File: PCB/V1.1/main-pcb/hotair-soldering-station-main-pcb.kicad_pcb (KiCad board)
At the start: 2 copper layers, 89.4 x 90.9 mm, 84 parts, among them J1 230VAC_IN, J10 SOLD_IRON (r.2,54), J13 ICP (goldpin r2,54), J2 main-board-conn, J3 EARTH_GND, J4 24V_IN (NS-25 r2,54), J5 PSUPPLY (PWZ-02S r.3,96), J6 HOTAIR_FAN (JST r,2,54), J7 HOTAIR_MEAS (JST r.2,5), J8 HOTAIR_HEATER (PWZ-02S r.3,96), J9 SOLD_IRON (r.2,54), Q1 BC817, Q10 FP3055LP, Q2 BC807, Q3 BC817, Q4 Q_PMOS_GDS, Q5 BC817, Q6 BT139-600, Q7 BC817, Q8 FP3055LP, Q9 BC817, U1 MOC3041M, U2 MAX31855KASA, U3 MP1584-Step-Down, U4 AP1117-ADJ, U5 STM32F030K6Tx, U6 LM358, U7 MAX31855KASA, U8 STM32F103C6Tx

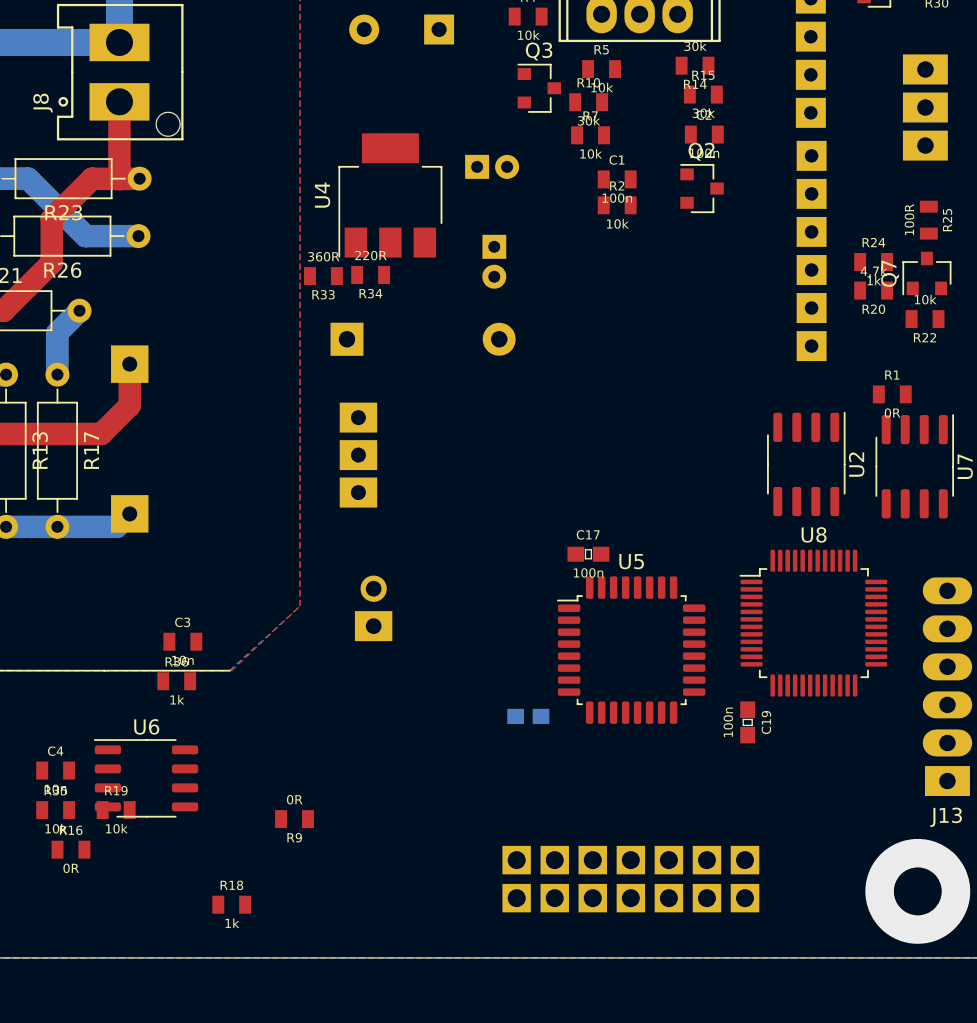
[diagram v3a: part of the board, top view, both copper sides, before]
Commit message: Pin assign to new STM32F103, front panel design to new case
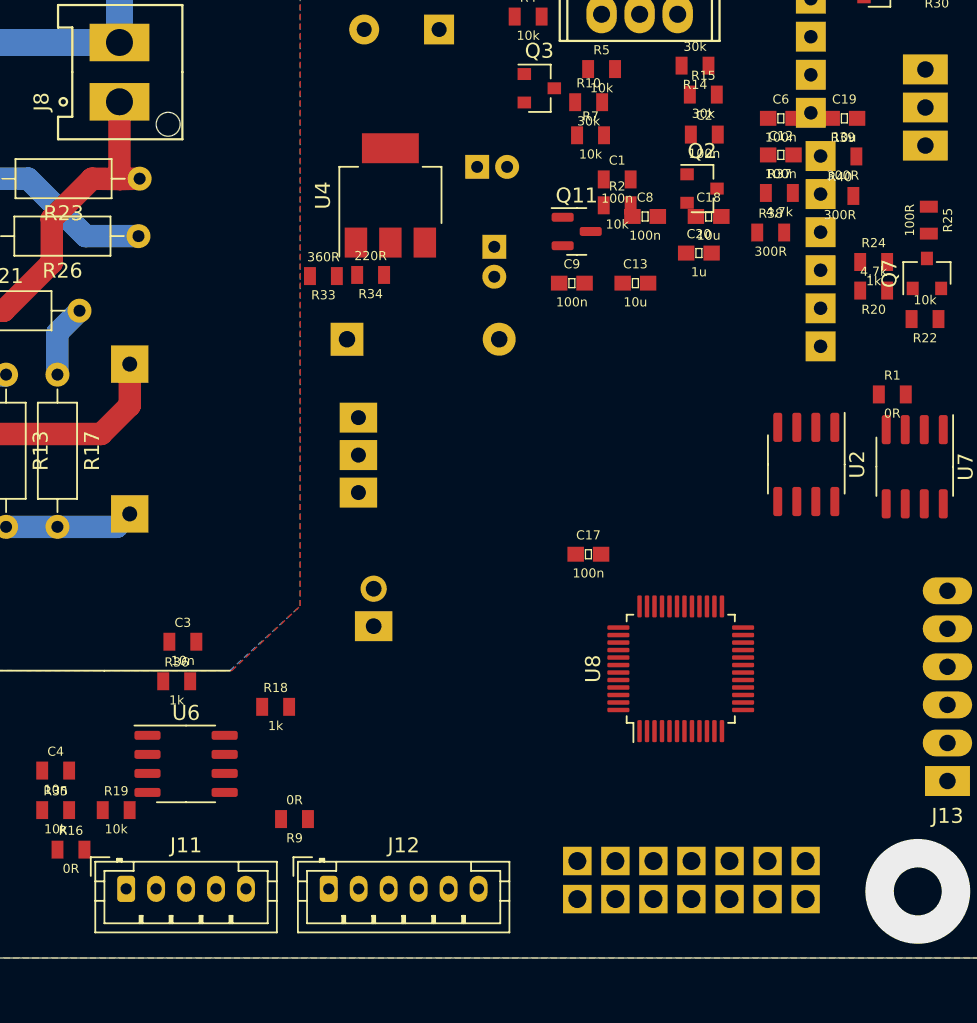
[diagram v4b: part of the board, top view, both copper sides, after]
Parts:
- removed U5: STM32F030K6Tx, Package_QFP:LQFP-32_7x7mm_P0.8mm
- added C12: 100n, Capacitors:0603, F.Cu at (92.4, 55.2)
- added C13: 10u, Capacitors:0603, F.Cu at (82.7, 63.8)
- added C20: 1u, Capacitors:0603, F.Cu at (86.9, 61.8)
- added C6: 100n, Capacitors:0603, F.Cu at (92.4, 52.8)
- added C8: 100n, Capacitors:0603, F.Cu at (83.3, 59.3)
- added C9: 100n, Capacitors:0603, F.Cu at (78.5, 63.8)
- added J11: LCD_CON2 (JST r.2.0), Connector_JST:JST_PH_B5B-PH-K_1x05_P2.00mm_Vertical, F.Cu at (48.7, 104.2)
- added J12: LCD_CON1 (JST r.2.0), Connector_JST:JST_PH_B6B-PH-K_1x06_P2.00mm_Vertical, F.Cu at (62.2, 104.2)
- added Q11: BC817, Package_TO_SOT_SMD:SOT-23, F.Cu at (78.8, 60.3)
- added R37: 4,7k, Capacitors:0805, F.Cu at (92.3, 57.8)
- added R38: 300R, Capacitors:0805, F.Cu at (91.7, 60.4)
- added R39: 300R, Capacitors:0805, F.Cu at (96.5, 55.3)
- added R40: 300R, Capacitors:0805, F.Cu at (96.3, 58.0)
- C18: value 100n -> 10u; moved to F.Cu
- C19: value 100n -> 10u
- J2: value main-board-conn -> FRONT_PANEL (IDC r. 2,54)
- moved C19 40.8 mm to (96.6, 52.8), turned to 0 degrees
- moved C18 35.5 mm to (87.6, 59.3)
- moved R18 13.5 mm to (58.7, 92.1)
- moved U8 9.40 mm to (85.7, 89.5), turned to 90 degrees
- moved J2 4.05 mm to (77.1, 100.5)
- moved U6 2.81 mm to (52.7, 95.9)
- moved J9 0.60 mm to (91.8, 54.0)
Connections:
- net HOTAIR_ADC renamed HOTAIR_TEMP_ADC
- C2 pad 1: FAN_ADC -> HOTAIR_FAN_ADC
- J10 pad 4: IRON_T12_HEATER -> IRON_T12_MOTION_SW
- J2 pad 10: HOTAIR_ON_SW -> HOTAIR_UP_SW
- J2 pad 11: SOLDER_ON_SW -> HOTAIR_DOWN_SW
- J2 pad 12: SPI1_SCK -> SOLDER_SELECT_SW
- J2 pad 13: (no net) -> HOTAIR_ON_SW
- J2 pad 14: SPI1_MOSI -> SOLDER_ON_SW
- J2 pad 3: GND -> MENU_UP_SW
- J2 pad 4: SOLDER_DOWN_SW -> MENU_OK_SW
- J2 pad 5: SOLDER_UP_SW -> MENU_DOWN_SW
- J2 pad 6: HOTAIR_DOWN_SW -> SOLDER_DOWN_SW
- J2 pad 7: HOTAIR_UP_SW -> SOLDER_UP_SW
- R14 pad 1: FAN_ADC -> HOTAIR_FAN_ADC
- R15 pad 2: FAN_ADC -> HOTAIR_FAN_ADC
- R2 pad 1: FAN_PWM -> HOTAIR_FAN_PWM
- R36 pad 2: IRON_T12_ADC -> IRON_T12_TEMP_ADC
- U1 pad 3: (no net) -> unconnected-(U1-Pad3)
- U1 pad 5: (no net) -> unconnected-(U1-Pad5)
- U7 pad 6: (no net) -> MAX31855_IRON_WEP_CS
- U8 pad 1: (no net) -> +3V3
- U8 pad 10: IRON_T12_ADC -> HOTAIR_FAN_ADC
- U8 pad 12: SOLDER_DOWN_SW -> UART_DBG_TX
- U8 pad 13: FAN_ADC -> MAX31855_HOTAIR_CS
- U8 pad 14: BUZZER -> MAX31855_IRON_CS
- U8 pad 17: SPI1_MOSI -> IRON_WEP_HEATER_CTRL
- U8 pad 18: SOLDER_ON_SW -> IRON_T12_TEMP_ADC
- U8 pad 19: HOTAIR_REED_SW -> IRON_T12_MOTION_SW
- U8 pad 2: (no net) -> LCD_RW
- U8 pad 20: (no net) -> HOTAIR_REED_SW
- U8 pad 21: (no net) -> SOLDER_ON_SW
- U8 pad 22: (no net) -> SOLDER_UP_SW
- U8 pad 25: (no net) -> SOLDER_DOWN_SW
- U8 pad 26: (no net) -> SOLDER_SELECT_SW
- U8 pad 27: (no net) -> HOTAIR_DOWN_SW
- U8 pad 28: (no net) -> HOTAIR_UP_SW
- U8 pad 29: HOTAIR_UP_SW -> HOTAIR_FAN_PWM
- U8 pad 3: (no net) -> LCD_RS
- U8 pad 30: UART_DBG_TX -> HOTAIR_HEATER_CTRL
- U8 pad 31: HOTAIR_FAN_UP_SW -> MENU_UP_SW
- U8 pad 32: HOTAIR_FAN_DOWN_SW -> MENU_OK_SW
- U8 pad 33: HOTAIR_ON_SW -> MENU_DOWN_SW
- U8 pad 38: MAX31855_HOTAIR_CS -> BUZZER
- U8 pad 39: SOLDER_UP_SW -> LCD_BACKLIGHT_PWM
- U8 pad 4: (no net) -> HOTAIR_FAN_DOWN_SW
- U8 pad 40: HOTAIR_DOWN_SW -> LCD_D7
- U8 pad 41: (no net) -> LCD_D6
- U8 pad 42: IRON_WEP_HEATER_CTRL -> IRON_T12_HEATER_CTRL
- U8 pad 43: FAN_PWM -> LCD_D5
- U8 pad 44: GND -> unconnected-(U8-Pad44)
- U8 pad 45: IRON_T12_HEATER_CTRL -> LCD_D4
- U8 pad 46: HOTAIR_HEATER_CTRL -> LCD_EN
- U8 pad 5: (no net) -> HOTAIR_ON_SW
- U8 pad 6: (no net) -> HOTAIR_FAN_UP_SW
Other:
- net class 230V removed
- net class Default removed
- net class gnd removed
- net class uC removed
